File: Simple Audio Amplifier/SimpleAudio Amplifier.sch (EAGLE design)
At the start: 8 parts, among them IC1 TDA7052A, IC2 TDA7053A

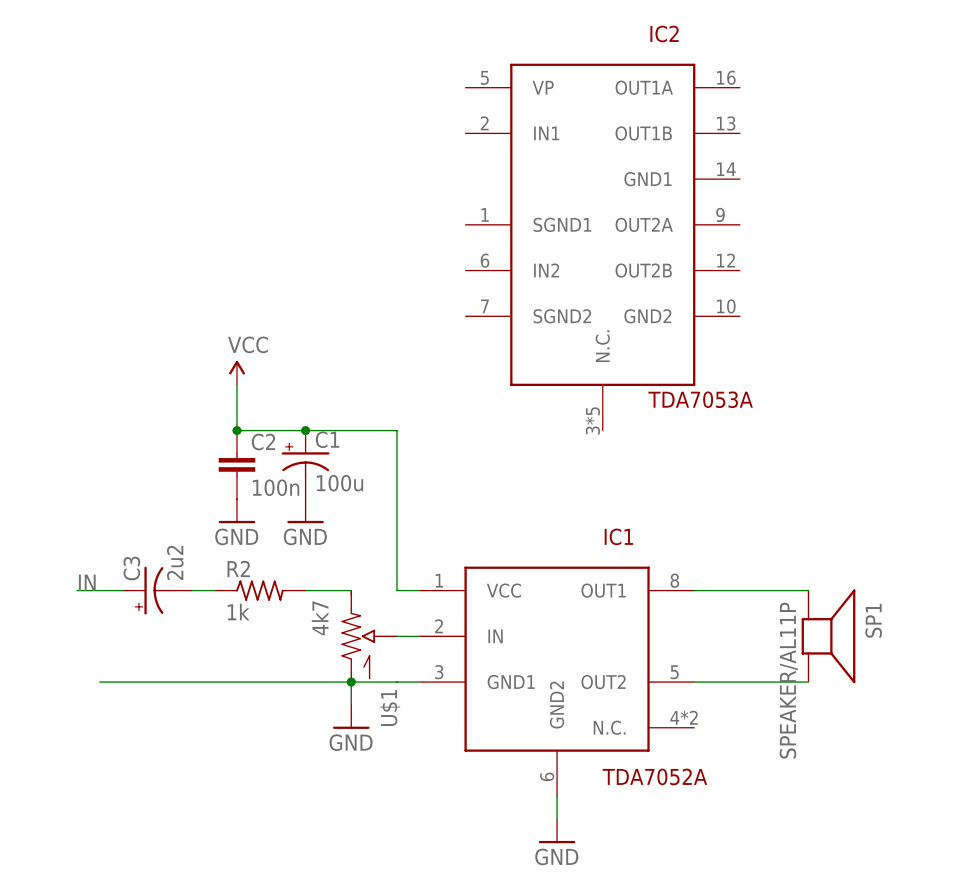
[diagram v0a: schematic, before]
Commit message: MyLibrary, Amplifier
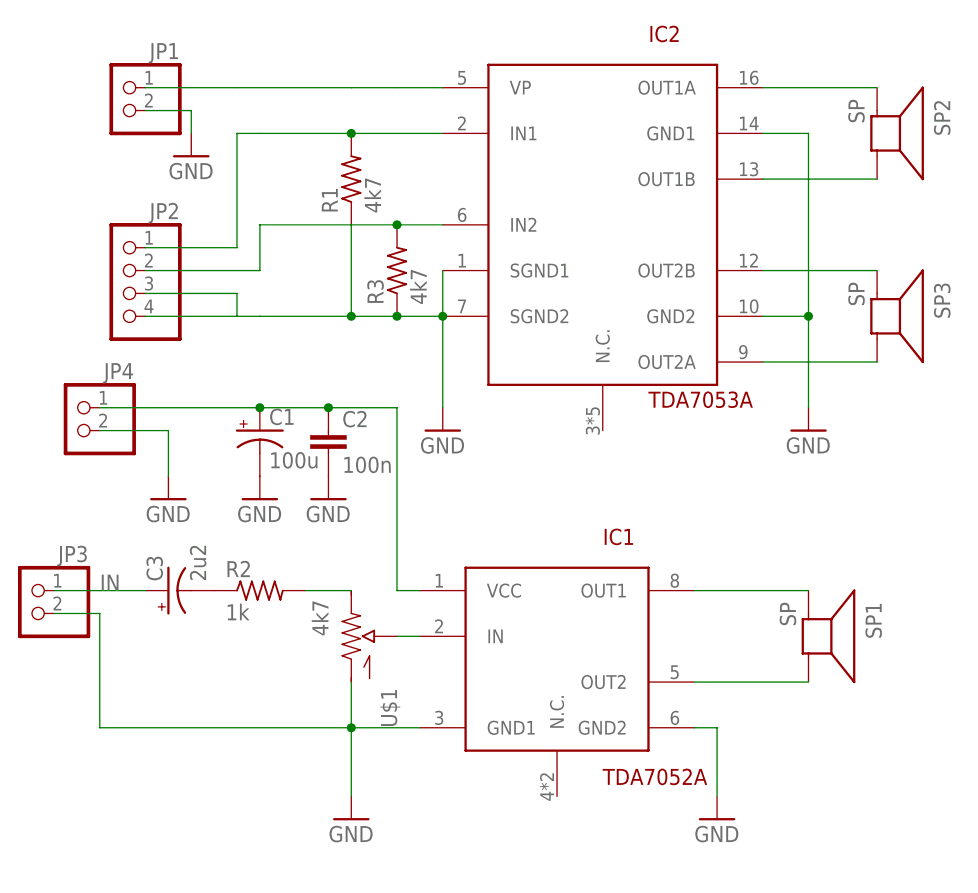
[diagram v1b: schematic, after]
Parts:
- added JP1, JP3, JP4: (no value), pinhead:PINHD-1X2
- added JP2: (no value), pinhead:PINHD-1X4
- added R1, R3: 4k7, adafruit:R-US_0204/5
- added SP2, SP3: SP, My Library:SP
- SP1: value SPEAKER/AL11P -> SP; device adafruit:SPEAKER/AL11P -> My Library:SP
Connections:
- removed net VCC: C1.+, C2.1, IC1.VCC
- new net N$1: C1.+, C2.1, IC1.VCC, JP4.1
- new net N$10: IC2.OUT2B, SP3.+
- new net N$11: IC2.OUT1B, SP2.-
- new net N$12: IC2.OUT1A, SP2.+
- new net N$17: IC2.VP, JP1.1
- new net N$4: IC2.IN1, JP2.1, R1.2
- new net N$6: IC2.IN2, JP2.2, R3.2
- new net N$7: IC2.OUT2A, SP3.-
- net GND: now also IC2.GND1, IC2.GND2, IC2.SGND1, IC2.SGND2, JP1.2, JP2.3, JP2.4, JP3.2, JP4.2, R1.1, R3.1
- net IN: now also JP3.1
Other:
- moved on the sheet: C1, C2, C3, IC1
